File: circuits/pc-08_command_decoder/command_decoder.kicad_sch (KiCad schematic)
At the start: 34 parts, among them J1 Screw_Terminal_01x02, J2 Conn_01x05, J3 Conn_01x03, J4 Conn_01x08, J5 Conn_01x05, J6 Conn_01x07, U1 74HC138, U2 74HC138, U3 74HC138, U4 74HC138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

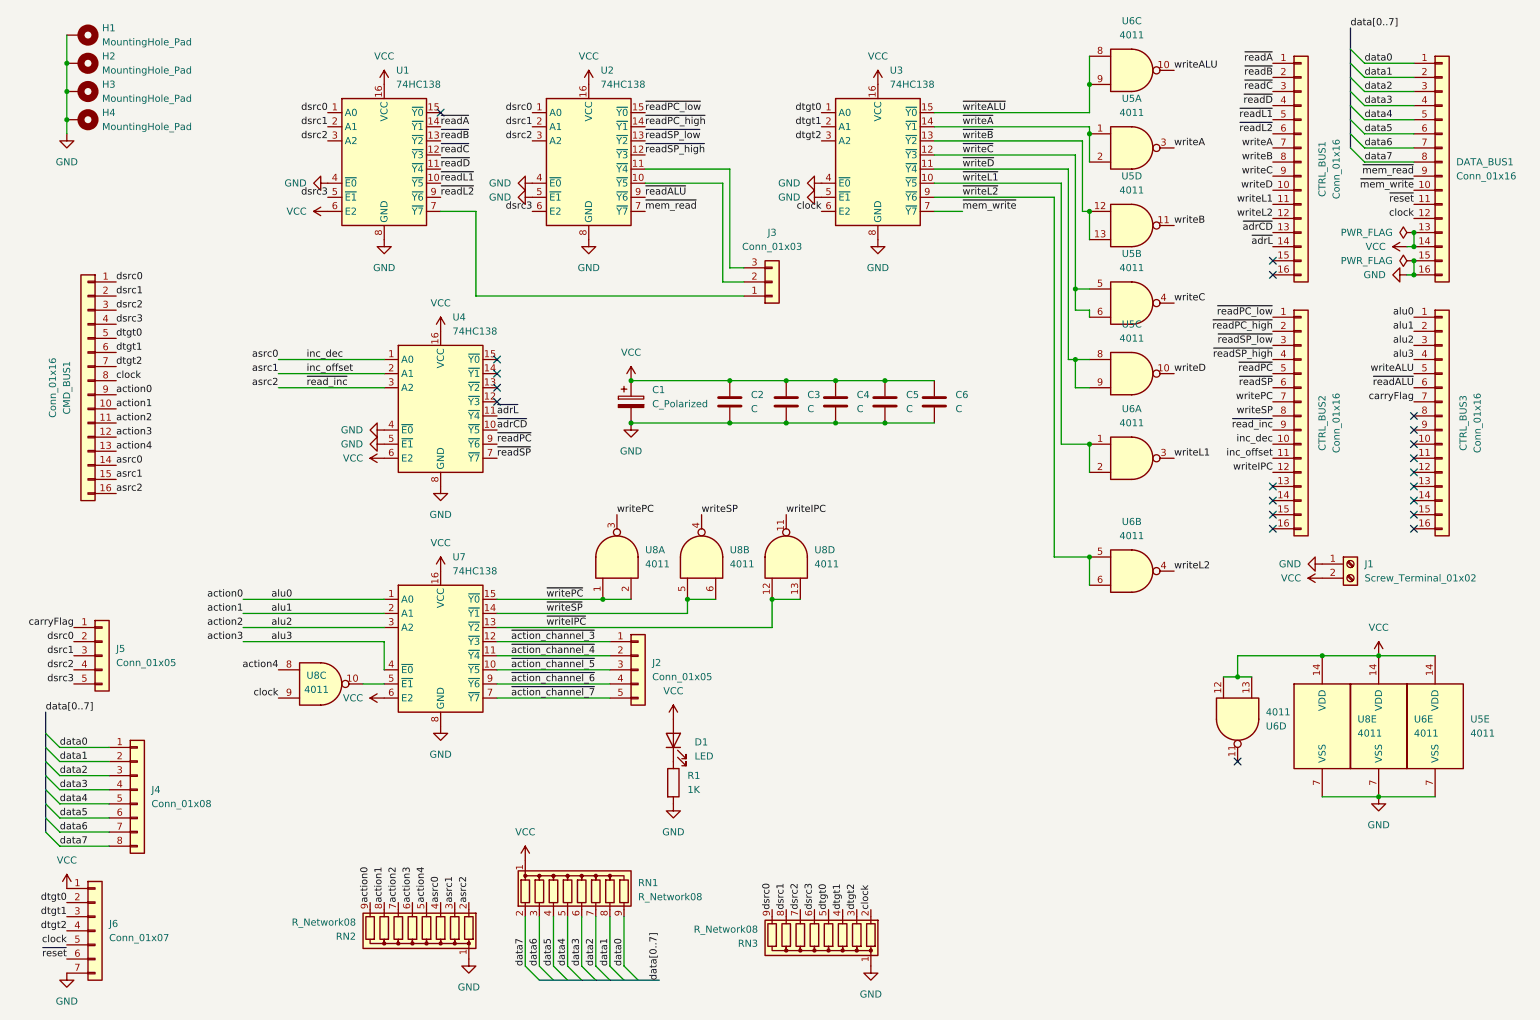
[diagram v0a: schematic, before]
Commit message: update documentation and update PCBs for interrupts
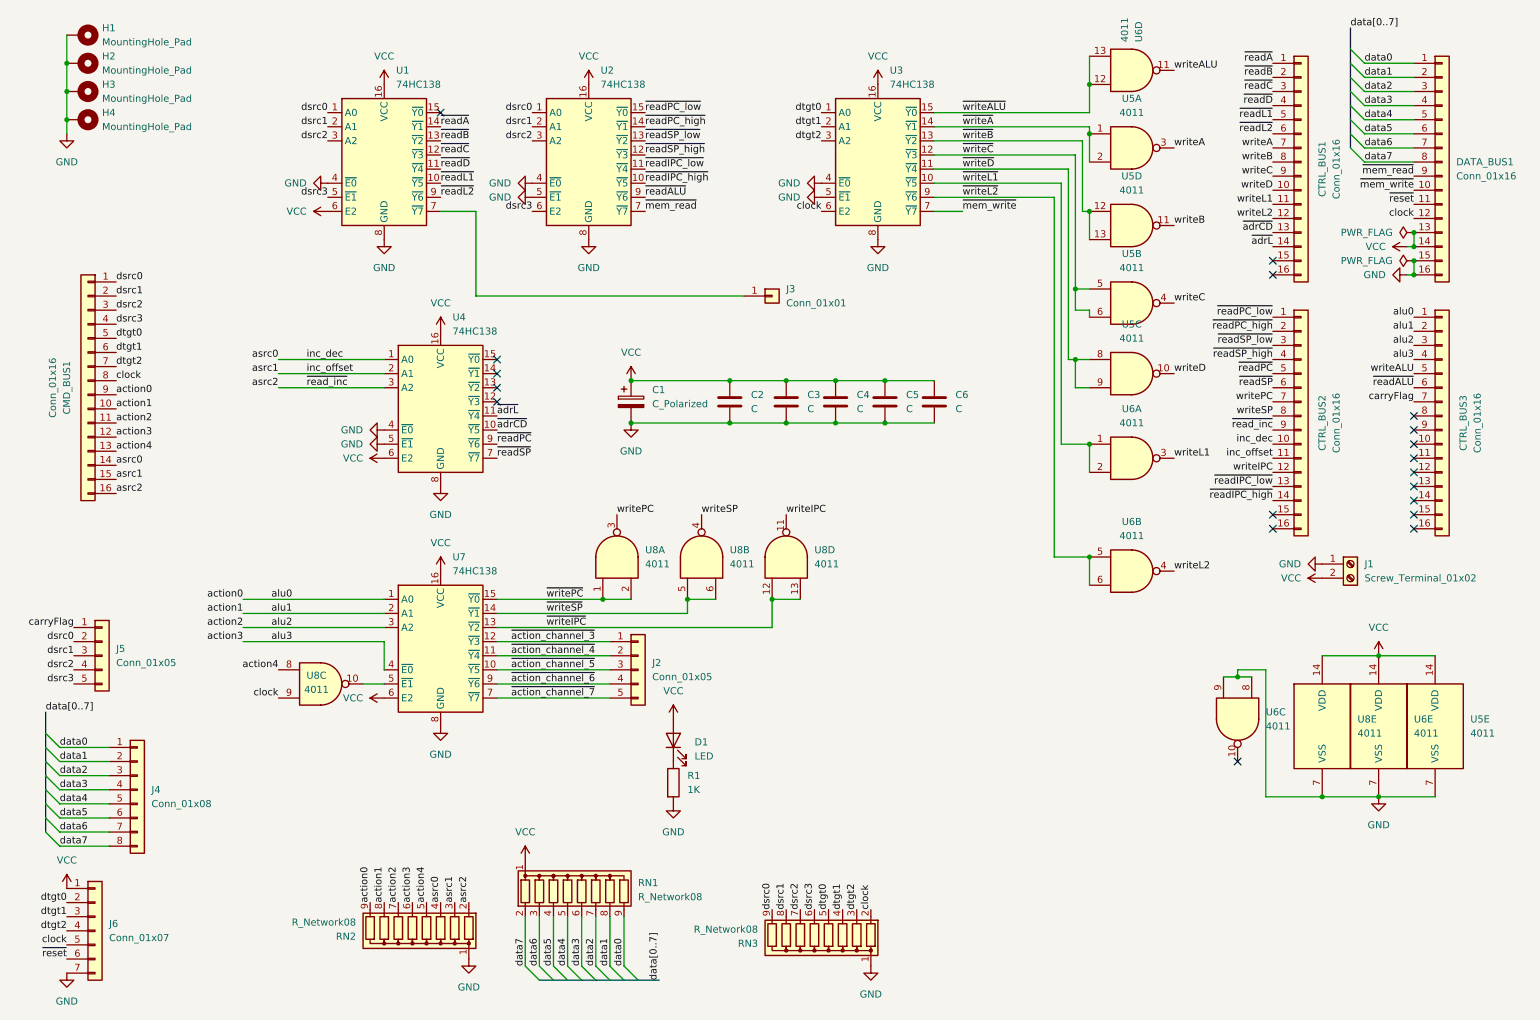
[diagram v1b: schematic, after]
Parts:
- removed J3: Conn_01x03, Connector_PinHeader_2.54mm:PinHeader_1x03_P2.54mm_Vertical, symbol Connector_Generic:Conn_01x03
- added J3: Conn_01x01, Connector_PinHeader_2.54mm:PinHeader_1x01_P2.54mm_Vertical, symbol Connector_Generic:Conn_01x01
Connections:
- net GND: now also U6.8, U6.9
- net VCC: no longer U6.12, U6.13
- net writeALU: now also U6.11; no longer U6.10
- net ~{writeALU}: now also U6.12, U6.13; no longer U6.8, U6.9
- net at U1.7 (~{Y7}): now also J3.1 (Pin_1)
- net ~{readIPC_low}: now reaches CTRL_BUS2.13 (Pin_13)
- net ~{readIPC_low}: now also U2.11 (~{Y4})
- net ~{readIPC_high}: now reaches CTRL_BUS2.14 (Pin_14)
- net ~{readIPC_high}: now also U2.10 (~{Y5})
- no-connect marks 21 -> 19
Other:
- moved on the sheet: U6C, U6D
